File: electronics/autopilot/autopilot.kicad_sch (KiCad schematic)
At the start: 5 parts

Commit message: autopilot board almost finished
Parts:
- added AE1: Antenna, symbol Device:Antenna
- added C1, C3: 100n, symbol Device:C_Small
- added C2: 4.7u, symbol Device:C_Small
- added J1, J2, J3, J4: Conn_01x03_Male, symbol Connector:Conn_01x03_Male
- added J5: Conn_01x02_Female, symbol Connector:Conn_01x02_Female
- added J6: GSM_MODULE, symbol Connector:Conn_01x07_Female
- added J8: MPPT_I2C, symbol Connector:Conn_01x02_Female
- added R3, R4: 100, symbol Device:R_Small
- added U2: SIM28ML, RF_GPS:SIM28ML, symbol RF_GPS:SIM28ML
- added U3: NRF24L01_Breakout, RF_Module:nRF24L01_Breakout, symbol RF:NRF24L01_Breakout
- added U4: 74HC244, symbol 74xx:74HC244
- J9: renamed from J?; value I2C -> IMU_I2C
- R1: renamed from R?; value R_Small -> 33k
- R2: renamed from R?; value R_Small -> 68k
- gave numbers to parts that had none: 2
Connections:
- net +5V: now also U1.40 (VBUS), J1.2 (Pin_2), J2.2 (Pin_2), J3.2 (Pin_2), J4.2 (Pin_2), J6.1 (Pin_1), U4.20 (VCC)
- net GND: now also U1.13 (GND), U1.18 (GND), U1.23 (GND), U1.28 (GND), U1.3 (GND), U1.33 (AGND), U1.38 (GND), U1.42 (GND), U1.8 (GND), C1.2, C2.2, C3.2, J1.1 (Pin_1), J2.1 (Pin_1), J3.1 (Pin_1), J4.1 (Pin_1), J5.2 (Pin_2), J6.2 (Pin_2), J6.6 (Pin_6), U2.1 (GND), U2.10 (GND), U2.12 (GND), U3.1 (GND), U4.1 (1OE), U4.10 (GND), U4.19 (2OE)
- net IBUS: now also U1.12 (GPIO9); no longer U1.2 (GPIO1)
- net at J9.1 (Pin_1): now also U1.6 (GPIO4)
- net at J9.2 (Pin_2): now also U1.7 (GPIO5)
- net GPS_RX: now reaches U1.1 (GPIO0)
- net GPS_RX: now also J6.5 (Pin_5), R4.1
- net at U1.10 (GPIO7): now also J8.2 (Pin_2)
- net PWM_SERVO1: now reaches U1.14 (GPIO10)
- net PWM_SERVO1: now also U4.2 (1A0)
- net PWM_SERVO2: now reaches U1.15 (GPIO11)
- net PWM_SERVO2: now also U4.4 (1A1)
- net PWM_SERVO3: now reaches U1.16 (GPIO12)
- net PWM_SERVO3: now also U4.6 (1A2)
- net PWM_SERVO4: now reaches U1.17 (GPIO13)
- net PWM_SERVO4: now also U4.8 (1A3)
- net PWM_ESC: now reaches U1.19 (GPIO14)
- net PWM_ESC: now also U4.17 (2A0)
- net MISO: now reaches U1.21 (GPIO16)
- net MISO: now also U3.7 (MISO)
- net CE: now reaches U1.22 (GPIO17)
- net CE: now also U3.3 (CE)
- net SCK: now reaches U1.24 (GPIO18)
- net SCK: now also U3.5 (SCK)
- net MOSI: now reaches U1.25 (GPIO19)
- net MOSI: now also U3.6 (MOSI)
- net CSN: now reaches U1.26 (GPIO20)
- net CSN: now also U3.4 (~{CSN})
- net +3.3V: now reaches U1.36 (3V3)
- net +3.3V: now also C1.1, C2.1, C3.1, J6.3 (Pin_3), U2.8 (Vcc), U3.2 (VCC)
- net GPS_RST: now reaches U1.4 (GPIO2)
- net GPS_RST: now also J6.7 (Pin_7)
- net at U1.9 (GPIO6): now also J8.1 (Pin_1)
- new net: AE1.1 (A), U2.11 (RF_IN)
- new net: R3.2, U2.2 (TXD0)
- new net: R4.2, U2.3 (RXD0)
- new net ESC: J5.1 (Pin_1), U4.3 (2Y0)
- new net GPS_TX: J6.4 (Pin_4), R3.1, U1.2 (GPIO1)
- new net SERVO1: J1.3 (Pin_3), U4.18 (1Y0)
- new net SERVO2: J2.3 (Pin_3), U4.16 (1Y1)
- new net SERVO3: J3.3 (Pin_3), U4.14 (1Y2)
- new net SERVO4: J4.3 (Pin_3), U4.12 (1Y3)
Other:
- moved on the sheet: J7, J9, R1, R2, U1

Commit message: autopilot schematic first version
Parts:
- removed J8: MPPT_I2C, symbol Connector:Conn_01x02_Female
- removed J9: IMU_I2C, symbol Connector:Conn_01x02_Female
- added D1: LED, LED_SMD:LED_1206_3216Metric_Pad1.42x1.75mm_HandSolder, symbol Device:LED
- added J10: Conn_01x03_Female, Connector_PinHeader_2.54mm:PinHeader_1x03_P2.54mm_Vertical, symbol Connector:Conn_01x03_Female
- added J11: Debug, Connector_PinHeader_2.54mm:PinHeader_1x03_P2.54mm_Vertical, symbol Connector:Conn_01x03_Male
- added J8: Screw_Terminal_01x02, moje:ARK, symbol Connector:Screw_Terminal_01x02
- added J9: Conn_01x08_Female, Connector_PinHeader_2.54mm:PinHeader_1x08_P2.54mm_Vertical, symbol Connector:Conn_01x08_Female
- added R5: 10k, Resistor_SMD:R_1206_3216Metric_Pad1.30x1.75mm_HandSolder, symbol Device:R_Small
- AE1: footprint (none) -> Connector_PinHeader_2.54mm:PinHeader_1x01_P2.54mm_Vertical
- C1, C2, C3: footprint (none) -> Capacitor_SMD:C_1206_3216Metric_Pad1.33x1.80mm_HandSolder
- J1, J2, J3, J4, J7: footprint (none) -> Connector_PinHeader_2.54mm:PinHeader_1x03_P2.54mm_Vertical
- J5: footprint (none) -> Connector_PinHeader_2.54mm:PinHeader_1x02_P2.54mm_Vertical
- J6: footprint (none) -> Connector_PinHeader_2.54mm:PinHeader_1x07_P2.54mm_Vertical
- R1, R2, R3, R4: footprint (none) -> Resistor_SMD:R_1206_3216Metric_Pad1.30x1.75mm_HandSolder
- U4: footprint (none) -> Package_SO:HTSSOP-20-1EP_4.4x6.5mm_P0.65mm_EP2.85x4mm
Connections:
- net +3.3V: now also J9.1 (Pin_1), J9.2 (Pin_2), J9.6 (Pin_6)
- net +5V: now also J8.1 (Pin_1)
- net GND: now also D1.1 (K), J10.3 (Pin_3), J8.2 (Pin_2), J9.3 (Pin_3), J9.7 (Pin_7); no longer U1.42 (GND)
- net GPS_RX: no longer J6.5 (Pin_5)
- net GPS_TX: no longer J6.4 (Pin_4)
- net IBUS: now also U1.20 (GPIO15); no longer U1.12 (GPIO9)
- net MPPT_I2C_SDA: now reaches U1.9 (GPIO6)
- net MPPT_I2C_SDA: now also J10.2 (Pin_2)
- net MPPT_I2C_SCL: now reaches U1.10 (GPIO7)
- net MPPT_I2C_SCL: now also J10.1 (Pin_1)
- net IMU_I2C_SDA: now reaches U1.6 (GPIO4)
- net IMU_I2C_SDA: now also J9.5 (Pin_5)
- net IMU_I2C_SCL: now reaches U1.7 (GPIO5)
- net IMU_I2C_SCL: now also J9.4 (Pin_4)
- net GSM_RX: now reaches U1.11 (GPIO8)
- net GSM_RX: now also J6.5 (Pin_5)
- net LED: now reaches U1.27 (GPIO21)
- net LED: now also R5.2
- net at U1.41 (SWCLK): now also J11.1 (Pin_1)
- net at U1.43 (SWDIO): now also J11.3 (Pin_3)
- new net: D1.2 (A), R5.1
- new net: J11.2 (Pin_2), U1.42 (GND)
- new net GSM_TX: J6.4 (Pin_4), U1.12 (GPIO9)
- no-connect marks 0 -> 1
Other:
- moved on the sheet: J6

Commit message: autopilot board  finished
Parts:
- added L1: 27n, Inductor_SMD:L_1210_3225Metric_Pad1.42x2.65mm_HandSolder, symbol pspice:INDUCTOR
- added R6: 10, Resistor_SMD:R_1206_3216Metric_Pad1.30x1.75mm_HandSolder, symbol Device:R_Small
- J1, J2, J3, J4: value Conn_01x03_Male -> SERVO
- J10: value Conn_01x03_Female -> MPPT_I2C
- J5: value Conn_01x02_Female -> ESC
- J8: value Screw_Terminal_01x02 -> 5V IN
- J9: value Conn_01x08_Female -> IMU
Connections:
- net at AE1.1 (A), U2.11 (RF_IN): now also L1.2
- net at U2.14 (Vcc_RF): now also R6.1
- new net: L1.1, R6.2
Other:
- moved on the sheet: C1, C2

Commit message: power board schematic almost finished
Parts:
- added J12: 5V IN, moje:ARK, symbol Connector:Screw_Terminal_01x02
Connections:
- net +3.3V: now also J12.1 (Pin_1); no longer U1.36 (3V3)
- net GND: now also J12.2 (Pin_2)
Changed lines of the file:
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@@
+    (stroke (width 0) (type default) (color 0 0 0 0))
+  )
+  (wire (pts (xy 63.5 91.44) (xy 73.66 91.44))
     (stroke (width 0) (type default) (color 0 0 0 0))
   )
@@
     (stroke (width 0) (type default) (color 0 0 0 0))
   )
-  (wire (pts (xy 167.64 41.91) (xy 167.64 43.18))
-    (stroke (width 0) (type default) (color 0 0 0 0))
-  )
   (wire (pts (xy 119.38 66.04) (xy 124.46 66.04))
     (stroke (width 0) (type default) (color 0 0 0 0))
@@
     (stroke (width 0) (type default) (color 0 0 0 0))
   )
+  (wire (pts (xy 63.5 93.98) (xy 73.66 93.98))
+    (stroke (width 0) (type default) (color 0 0 0 0))
+  )
   (wire (pts (xy 36.83 161.29) (xy 34.29 161.29))
     (stroke (width 0) (type default) (color 0 0 0 0))
@@
     (stroke (width 0) (type default) (color 0 0 0 0))
   )
+  (wire (pts (xy 73.66 95.25) (xy 73.66 93.98))
+    (stroke (width 0) (type default) (color 0 0 0 0))
+  )
   (wire (pts (xy 41.91 63.5) (xy 45.72 63.5))
     (stroke (width 0) (type default) (color 0 0 0 0))
@@
     (stroke (width 0) (type default) (color 0 0 0 0))
   )
+  (wire (pts (xy 73.66 88.9) (xy 73.66 91.44))
+    (stroke (width 0) (type default) (color 0 0 0 0))
+  )
   (wire (pts (xy 191.77 77.47) (xy 191.77 80.01))
     (stroke (width 0) (type default) (color 0 0 0 0))
@@
   )
   (wire (pts (xy 240.03 29.21) (xy 248.92 29.21))
-    (stroke (width 0) (type default) (color 0 0 0 0))
-  )
-  (wire (pts (xy 160.02 43.18) (xy 167.64 43.18))
     (stroke (width 0) (type default) (color 0 0 0 0))
   )
@@
     (pin "2")
   )
+  (symbol (lib_id "power:GND") (at 73.66 95.25 0) (unit 1)
+    (in_bom yes) (on_board yes) (fields_autoplaced)
+    (property "Reference" "#PWR0101" (id 0) (at 73.66 101.6 0)
+      (effects (font (size 1.27 1.27)) hide)
+    )
+    (property "Value" "GND" (id 1) (at 73.66 100.33 0))
+    (property "Footprint" "" (id 2) (at 73.66 95.25 0)
+      (effects (font (size 1.27 1.27)) hide)
+    )
+    (property "Datasheet" "" (id 3) (at 73.66 95.25 0)
+      (effects (font (size 1.27 1.27)) hide)
+    )
+    (pin "1")
+  )
   (symbol (lib_id "power:GND") (at 175.26 76.2 0) (unit 1)
     (in_bom yes) (on_board yes) (fields_autoplaced)
@@
     (pin "1")
   )
-  (symbol (lib_id "power:+3.3V") (at 167.64 41.91 0) (unit 1)
-    (in_bom yes) (on_board yes) (fields_autoplaced)
-    (property "Reference" "#PWR022" (id 0) (at 167.64 45.72 0)
-      (effects (font (size 1.27 1.27)) hide)
-    )
-    (property "Value" "+3.3V" (id 1) (at 167.64 36.83 0))
-    (property "Footprint" "" (id 2) (at 167.64 41.91 0)
-      (effects (font (size 1.27 1.27)) hide)
-    )
-    (property "Datasheet" "" (id 3) (at 167.64 41.91 0)
+  (symbol (lib_id "power:+3.3V") (at 73.66 88.9 0) (unit 1)
+    (in_bom yes) (on_board yes) (fields_autoplaced)
+    (property "Reference" "#PWR022" (id 0) (at 73.66 92.71 0)
+      (effects (font (size 1.27 1.27)) hide)
+    )
+    (property "Value" "+3.3V" (id 1) (at 73.66 83.82 0))
+    (property "Footprint" "" (id 2) (at 73.66 88.9 0)
+      (effects (font (size 1.27 1.27)) hide)
+    )
+    (property "Datasheet" "" (id 3) (at 73.66 88.9 0)
       (effects (font (size 1.27 1.27)) hide)
     )
@@
     )
     (property "Datasheet" "https://www.tme.eu/pl/details/smd1206-68k/rezystory-smd-1206/royal-ohm/1206s4j0683t5e/" (id 3) (at 151.13 168.91 0)
+      (effects (font (size 1.27 1.27)) hide)
+    )
+    (pin "1")
+    (pin "2")
+  )
+  (symbol (lib_id "Connector:Screw_Terminal_01x02") (at 58.42 91.44 0) (mirror y) (unit 1)
+    (in_bom yes) (on_board yes) (fields_autoplaced)
+    (property "Reference" "J12" (id 0) (at 58.42 85.09 0))
+    (property "Value" "5V IN" (id 1) (at 58.42 87.63 0))
+    (property "Footprint" "moje:ARK" (id 2) (at 58.42 91.44 0)
+      (effects (font (size 1.27 1.27)) hide)
+    )
+    (property "Datasheet" "https://www.tme.eu/pl/details/tb-5.0-p-2p/listwy-zaciskowe-do-druku/ninigi/" (id 3) (at 58.42 91.44 0)
       (effects (font (size 1.27 1.27)) hide)
     )
@@
       (reference "#PWR039") (unit 1) (value "GND") (footprint "")
     )
+    (path "/4a8b7425-4083-48cc-83b6-e622cb8f6444"
+      (reference "#PWR0101") (unit 1) (value "GND") (footprint "")
+    )
     (path "/31a915df-d94a-4c5d-a919-8d4fe132c8c9"
       (reference "AE1") (unit 1) (value "Antenna") (footprint "Connector_PinHeader_2.54mm:PinHeader_1x01_P2.54mm_Vertical")
@@
       (reference "J11") (unit 1) (value "Debug") (footprint "Connector_PinHeader_2.54mm:PinHeader_1x03_P2.54mm_Vertical")
     )
+    (path "/af55ffb3-a8ad-455d-ad63-1cae0c75ac50"
+      (reference "J12") (unit 1) (value "5V IN") (footprint "moje:ARK")
+    )
     (path "/0175cbf4-b737-4ffc-b02e-49acda5e6f0a"

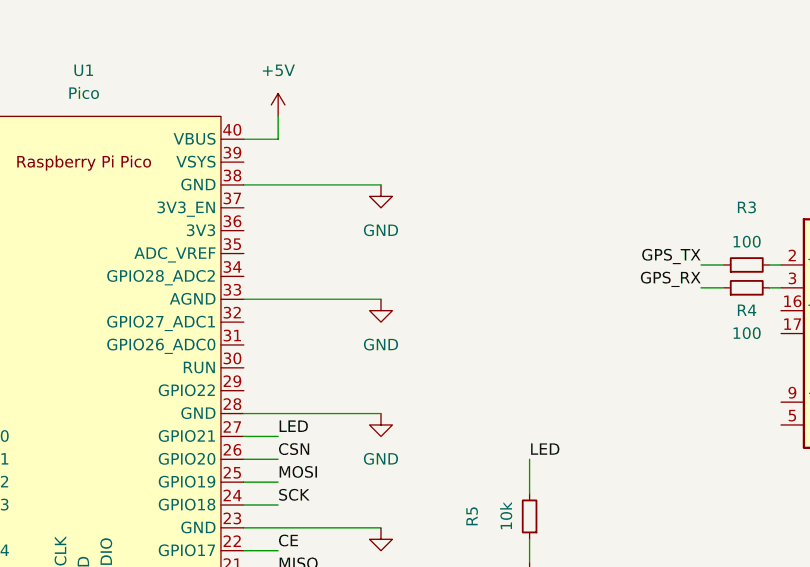
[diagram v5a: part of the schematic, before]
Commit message: links fixed
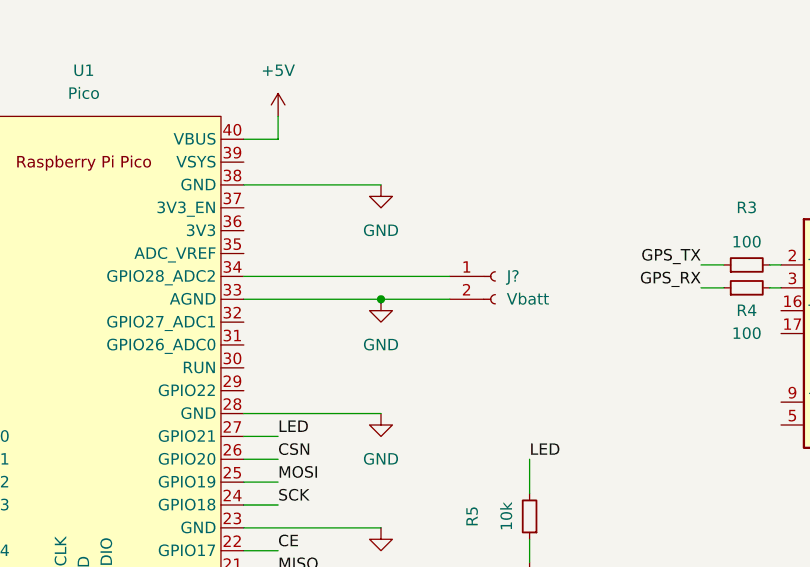
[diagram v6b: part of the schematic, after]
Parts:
- added J?: Vbatt, symbol Connector:Conn_01x02_Female
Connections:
- net GND: now also J?.2 (Pin_2)
- net at U1.34 (GPIO28_ADC2): now also J?.1 (Pin_1)
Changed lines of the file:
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@@
   (junction (at 34.29 163.83) (diameter 0) (color 0 0 0 0)
+  )
+  (junction (at 175.26 50.8) (diameter 0) (color 0 0 0 0)
   )
   (junction (at 128.27 97.79) (diameter 0) (color 0 0 0 0)
@@
     (stroke (width 0) (type default) (color 0 0 0 0))
   )
+  (wire (pts (xy 175.26 50.8) (xy 182.88 50.8))
+    (stroke (width 0) (type default) (color 0 0 0 0))
+  )
   (wire (pts (xy 63.5 91.44) (xy 73.66 91.44))
     (stroke (width 0) (type default) (color 0 0 0 0))
@@
   )
   (wire (pts (xy 63.5 110.49) (xy 73.66 110.49))
+    (stroke (width 0) (type default) (color 0 0 0 0))
+  )
+  (wire (pts (xy 160.02 48.26) (xy 182.88 48.26))
     (stroke (width 0) (type default) (color 0 0 0 0))
   )
@@
     )
     (pin "1")
+  )
+  (symbol (lib_id "Connector:Conn_01x02_Female") (at 187.96 48.26 0) (unit 1)
+    (in_bom yes) (on_board yes) (fields_autoplaced)
+    (property "Reference" "J?" (id 0) (at 189.23 48.2599 0)
+      (effects (font (size 1.27 1.27)) (justify left))
+    )
+    (property "Value" "Vbatt" (id 1) (at 189.23 50.7999 0)
+      (effects (font (size 1.27 1.27)) (justify left))
+    )
+    (property "Footprint" "" (id 2) (at 187.96 48.26 0)
+      (effects (font (size 1.27 1.27)) hide)
+    )
+    (property "Datasheet" "~" (id 3) (at 187.96 48.26 0)
+      (effects (font (size 1.27 1.27)) hide)
+    )
+    (pin "1")
+    (pin "2")
   )
   (symbol (lib_id "power:GND") (at 175.26 38.1 0) (unit 1)
@@
       (reference "J12") (unit 1) (value "5V IN") (footprint "moje:ARK")
     )
+    (path "/710045fb-f91b-414f-844b-e32080368dd7"
+      (reference "J?") (unit 1) (value "Vbatt") (footprint "")
+    )
     (path "/0175cbf4-b737-4ffc-b02e-49acda5e6f0a"
